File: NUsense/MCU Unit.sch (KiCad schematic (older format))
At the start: 40 parts

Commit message: Update NUsense Files
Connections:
- net GND: now also Y?.2 (GND1), Y?.4 (GND2)
- net USART1_TX: now reaches U?.101 (PA9)
- net USART1_RX: now reaches U?.102 (PA10)
- net JTMS_SWDIO: now reaches U?.105 (PA13)
- net JTCK_SWCLK: now reaches U?.109 (PA14)
- net JTDI: now reaches U?.110 (PA15)
- net USART3_TX: now reaches U?.111 (PC10)
- net USART3_RX: now reaches U?.112 (PC11)
- net UART5_TX: now reaches U?.113 (PC12)
- net JTDO_SWO: now reaches U?.133 (PB3)
- net OTG_HS_ULPI_D: now reaches U?.135 (PB5)
- net OTG_HS_ULPI_D: now also U?.37 (PA3), U?.46 (PB0), U?.47 (PB1), U?.69 (PB10), U?.70 (PB11), U?.73 (PB12), U?.74 (PB13)
- net MPU_SCL: now reaches U?.136 (PB6)
- net MPU_SDA/SDI: now reaches U?.137 (PB7)
- net MPU_INT: now reaches U?.139 (PB8)
- net OTG_HS_UPLI_STP: now reaches U?.26 (PC0)
- net OTG_HS_ULPI_DIR: now reaches U?.28 (PC2)
- net OTG_HS_UPLI_NXT: now reaches U?.29 (PC3)
- net OTG_HS_ULPI_CK: now reaches U?.41 (PA5)
- net USART6_TX: now reaches U?.96 (PC6)
- net USART6_RX: now reaches U?.97 (PC7)
- net UART5_RX: now reaches U?.116 (PD2)
- net USART2_TX: now reaches U?.119 (PD5)
- net USART2_RX: now reaches U?.122 (PD6)
- net UART8_RX: now reaches U?.141 (PE0)
- net UART8_TX: now reaches U?.142 (PE1)
- net UART7_RX: now reaches U?.58 (PE7)
- net UART7_TX: now reaches U?.59 (PE8)
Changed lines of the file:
@@
 LIBS:NUbots
 LIBS:STM32F746ZGT6
+LIBS:Header_Connectors
 LIBS:NUsense-cache
 EELAYER 25 0
@@
 $Descr A3 16535 11693
 encoding utf-8
-Sheet 3 4
+Sheet 3 9
 Title ""
 Date ""
@@
 	3800 6100 3800 5800
 Wire Wire Line
-	2850 6900 2700 6900
-Wire Wire Line
 	2700 6900 2700 7000
-Wire Wire Line
-	2600 7000 2850 7000
 Connection ~ 2700 7000
 Wire Wire Line
@@
 	1700 10100 3550 10100
 Connection ~ 3550 10100
+Text GLabel 5150 3200 0    60   Input ~ 0
+USART1_TX
+Text GLabel 5150 3300 0    60   Input ~ 0
+USART1_RX
+Text GLabel 6650 2900 2    60   Input ~ 0
+USART6_TX
+Text GLabel 6650 3000 2    60   Input ~ 0
+USART6_RX
+Text GLabel 6650 3300 2    60   Input ~ 0
+USART3_TX
+Text GLabel 6650 3400 2    60   Input ~ 0
+USART3_RX
+Text GLabel 6650 3500 2    60   Input ~ 0
+UART5_TX
+Text GLabel 12300 2500 0    60   Input ~ 0
+UART5_RX
+Text GLabel 12300 2800 0    60   Input ~ 0
+USART2_TX
+Text GLabel 12300 2900 0    60   Input ~ 0
+USART2_RX
+Text GLabel 12300 4000 0    60   Input ~ 0
+UART8_RX
+Text GLabel 12300 4100 0    60   Input ~ 0
+UART8_TX
+Text GLabel 12300 4700 0    60   Input ~ 0
+UART7_RX
+Text GLabel 12300 4800 0    60   Input ~ 0
+UART7_TX
+Text GLabel 5150 4600 0    60   Input ~ 0
+MPU_SCL
+Text GLabel 5150 4700 0    60   Input ~ 0
+MPU_SDA/SDI
+Text GLabel 5150 4800 0    60   Input ~ 0
+MPU_INT
+Text GLabel 5150 3600 0    60   Input ~ 0
+JTMS_SWDIO
+Text GLabel 5150 3700 0    60   Input ~ 0
+JTCK_SWCLK
+Text GLabel 5150 3800 0    60   Input ~ 0
+JTDI
+Text GLabel 5150 4300 0    60   Input ~ 0
+JTDO_SWO
+Text GLabel 5150 2600 0    60   Input ~ 0
+OTG_HS_ULPI_D
+Text GLabel 5150 4000 0    60   Input ~ 0
+OTG_HS_ULPI_D
+Text GLabel 5150 4100 0    60   Input ~ 0
+OTG_HS_ULPI_D
+Text GLabel 5150 4500 0    60   Input ~ 0
+OTG_HS_ULPI_D
+Text GLabel 5150 5000 0    60   Input ~ 0
+OTG_HS_ULPI_D
+Text GLabel 5150 5100 0    60   Input ~ 0
+OTG_HS_ULPI_D
+Text GLabel 5150 5200 0    60   Input ~ 0
+OTG_HS_ULPI_D
+Text GLabel 5150 5300 0    60   Input ~ 0
+OTG_HS_ULPI_D
+Text GLabel 5150 2800 0    60   Input ~ 0
+OTG_HS_ULPI_CK
+Text GLabel 6650 2300 2    60   Input ~ 0
+OTG_HS_UPLI_STP
+Text GLabel 6650 2500 2    60   Input ~ 0
+OTG_HS_ULPI_DIR
+Text GLabel 6650 2600 2    60   Input ~ 0
+OTG_HS_UPLI_NXT
+Wire Wire Line
+	2600 7000 2800 7000
+Wire Wire Line
+	2800 6900 2700 6900
 $EndSCHEMATC

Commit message: Change hierarchy layout
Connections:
- net JTDO_SWO renamed JTD0_SW0
- net MCU_NRESET renamed MCU_RESET
- net OTG_HS_UPLI_NXT renamed OTG_HS_ULPI_NXT
- net OTG_HS_UPLI_STP renamed OTG_HS_ULPI_STP
- net VDD3o3V renamed +3V3
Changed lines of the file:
@@
 LIBS:valves
 LIBS:ADM6713RAKS
+LIBS:Header_Connectors
 LIBS:MPU6000
 LIBS:NUbots
 LIBS:STM32F746ZGT6
-LIBS:Header_Connectors
 LIBS:NUsense-cache
 EELAYER 25 0
@@
 	0    -1   -1   0
 $EndComp
-Text GLabel 3250 7700 0    60   Input ~ 0
-MCU_NRESET
 $Comp
 L R R?
@@
 	1    0    0    -1
 $EndComp
-Text GLabel 5800 7500 2    60   Input ~ 0
-VDD3o3V
 $Comp
 L GND #PWR?
@@
 	1    0    0    -1
 $EndComp
-Text GLabel 6700 7000 1    60   Input ~ 0
-VDD3o3V
-Text GLabel 9200 8200 1    60   Input ~ 0
-VDD3o3V_MCU
 $Comp
 L Ferrite_Bead L?
@@
 	1    0    0    -1
 $EndComp
-Text GLabel 8250 8400 0    60   Input ~ 0
-VDD3o3V
 Text GLabel 8250 8850 0    60   Input ~ 0
 RTC_BAT
@@
 	0    1    1    0
 $EndComp
-Text GLabel 6900 9900 0    60   Input ~ 0
-VDD3o3V
 $Comp
 L GND #PWR?
@@
 	-1   0    0    1
 $EndComp
-Text GLabel 1300 9150 1    60   Input ~ 0
-VDD3o3V_MCU
 $Comp
 L GND #PWR?
@@
 	1700 10100 3550 10100
 Connection ~ 3550 10100
-Text GLabel 5150 3200 0    60   Input ~ 0
-USART1_TX
-Text GLabel 5150 3300 0    60   Input ~ 0
-USART1_RX
-Text GLabel 6650 2900 2    60   Input ~ 0
-USART6_TX
-Text GLabel 6650 3000 2    60   Input ~ 0
-USART6_RX
-Text GLabel 6650 3300 2    60   Input ~ 0
-USART3_TX
-Text GLabel 6650 3400 2    60   Input ~ 0
-USART3_RX
-Text GLabel 6650 3500 2    60   Input ~ 0
-UART5_TX
-Text GLabel 12300 2500 0    60   Input ~ 0
-UART5_RX
-Text GLabel 12300 2800 0    60   Input ~ 0
-USART2_TX
-Text GLabel 12300 2900 0    60   Input ~ 0
-USART2_RX
-Text GLabel 12300 4000 0    60   Input ~ 0
-UART8_RX
-Text GLabel 12300 4100 0    60   Input ~ 0
-UART8_TX
-Text GLabel 12300 4700 0    60   Input ~ 0
-UART7_RX
-Text GLabel 12300 4800 0    60   Input ~ 0
-UART7_TX
-Text GLabel 5150 4600 0    60   Input ~ 0
-MPU_SCL
-Text GLabel 5150 4700 0    60   Input ~ 0
-MPU_SDA/SDI
-Text GLabel 5150 4800 0    60   Input ~ 0
-MPU_INT
-Text GLabel 5150 3600 0    60   Input ~ 0
-JTMS_SWDIO
-Text GLabel 5150 3700 0    60   Input ~ 0
-JTCK_SWCLK
-Text GLabel 5150 3800 0    60   Input ~ 0
-JTDI
-Text GLabel 5150 4300 0    60   Input ~ 0
-JTDO_SWO
 Text GLabel 5150 2600 0    60   Input ~ 0
 OTG_HS_ULPI_D
@@
 Text GLabel 5150 5300 0    60   Input ~ 0
 OTG_HS_ULPI_D
-Text GLabel 5150 2800 0    60   Input ~ 0
+Wire Wire Line
+	2600 7000 2800 7000
+Wire Wire Line
+	2800 6900 2700 6900
+$Comp
+L +3.3V #PWR?
+U 1 1 5A6FCDF0
+P 6700 7000
+F 0 "#PWR?" H 6700 6850 50  0001 C CNN
+F 1 "+3.3V" H 6700 7140 50  0000 C CNN
+F 2 "" H 6700 7000 50  0001 C CNN
+F 3 "" H 6700 7000 50  0001 C CNN
+	1    6700 7000
+	1    0    0    -1
+$EndComp
+$Comp
+L +3.3V #PWR?
+U 1 1 5A6FCE7A
+P 5800 7500
+F 0 "#PWR?" H 5800 7350 50  0001 C CNN
+F 1 "+3.3V" H 5800 7640 50  0000 C CNN
+F 2 "" H 5800 7500 50  0001 C CNN
+F 3 "" H 5800 7500 50  0001 C CNN
+	1    5800 7500
+	0    1    1    0
+$EndComp
+$Comp
+L +3.3V #PWR?
+U 1 1 5A6FD08D
+P 6900 9900
+F 0 "#PWR?" H 6900 9750 50  0001 C CNN
+F 1 "+3.3V" H 6900 10040 50  0000 C CNN
+F 2 "" H 6900 9900 50  0001 C CNN
+F 3 "" H 6900 9900 50  0001 C CNN
+	1    6900 9900
+	0    -1   -1   0
+$EndComp
+$Comp
+L +3.3V #PWR?
+U 1 1 5A6FD2DC
+P 8250 8400
+F 0 "#PWR?" H 8250 8250 50  0001 C CNN
+F 1 "+3.3V" H 8250 8540 50  0000 C CNN
+F 2 "" H 8250 8400 50  0001 C CNN
+F 3 "" H 8250 8400 50  0001 C CNN
+	1    8250 8400
+	0    -1   -1   0
+$EndComp
+Text HLabel 5150 4800 0    60   Input ~ 0
+MPU_INT
+Text HLabel 5150 4700 0    60   Input ~ 0
+MPU_SDA/SDI
+Text HLabel 5150 4600 0    60   Input ~ 0
+MPU_SCL
+Text HLabel 3250 7700 0    60   Input ~ 0
+MCU_RESET
+Text HLabel 6650 2300 2    60   BiDi ~ 0
+OTG_HS_ULPI_STP
+Text HLabel 6650 2500 2    60   BiDi ~ 0
+OTG_HS_ULPI_DIR
+Text HLabel 6650 2600 2    60   BiDi ~ 0
+OTG_HS_ULPI_NXT
+Text HLabel 5150 2800 0    60   BiDi ~ 0
 OTG_HS_ULPI_CK
-Text GLabel 6650 2300 2    60   Input ~ 0
-OTG_HS_UPLI_STP
-Text GLabel 6650 2500 2    60   Input ~ 0
-OTG_HS_ULPI_DIR
-Text GLabel 6650 2600 2    60   Input ~ 0
-OTG_HS_UPLI_NXT
-Wire Wire Line
-	2600 7000 2800 7000
-Wire Wire Line
-	2800 6900 2700 6900
+Text Label 9200 8200 0    60   ~ 0
+VDD3o3V_MCU
+Text Label 1300 9150 0    60   ~ 0
+VDD3o3V_MCU
+Text HLabel 5150 4300 0    60   BiDi ~ 0
+JTD0_SW0
+Text HLabel 5150 3800 0    60   BiDi ~ 0
+JTDI
+Text HLabel 5150 3700 0    60   BiDi ~ 0
+JTCK_SWCLK
+Text HLabel 5150 3600 0    60   BiDi ~ 0
+JTMS_SWDIO
+Text HLabel 5150 3200 0    60   Output ~ 0
+USART1_TX
+Text HLabel 5150 3300 0    60   Input ~ 0
+USART1_RX
+Text HLabel 6650 2900 2    60   Output ~ 0
+USART6_TX
+Text HLabel 6650 3000 2    60   Input ~ 0
+USART6_RX
+Text HLabel 6650 3400 2    60   Input ~ 0
+USART3_RX
+Text HLabel 6650 3300 2    60   Output ~ 0
+USART3_TX
+Text HLabel 6650 3500 2    60   Output ~ 0
+UART5_TX
+Text HLabel 12300 2800 0    60   Output ~ 0
+USART2_TX
+Text HLabel 12300 2500 0    60   Input ~ 0
+UART5_RX
+Text HLabel 12300 4100 0    60   Output ~ 0
+UART8_TX
+Text HLabel 12300 2900 0    60   Input ~ 0
+USART2_RX
+Text HLabel 12300 4000 0    60   Input ~ 0
+UART8_RX
+Text HLabel 12300 4800 0    60   Output ~ 0
+UART7_TX
+Text HLabel 12300 4700 0    60   Input ~ 0
+UART7_RX
 $EndSCHEMATC

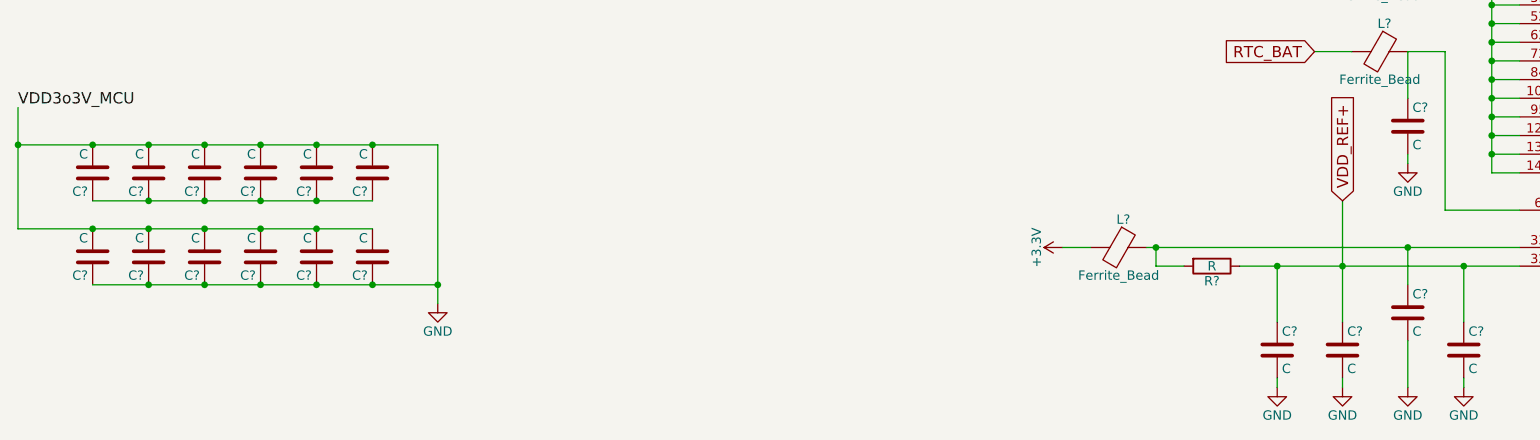
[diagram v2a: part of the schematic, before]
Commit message: Update Component Values
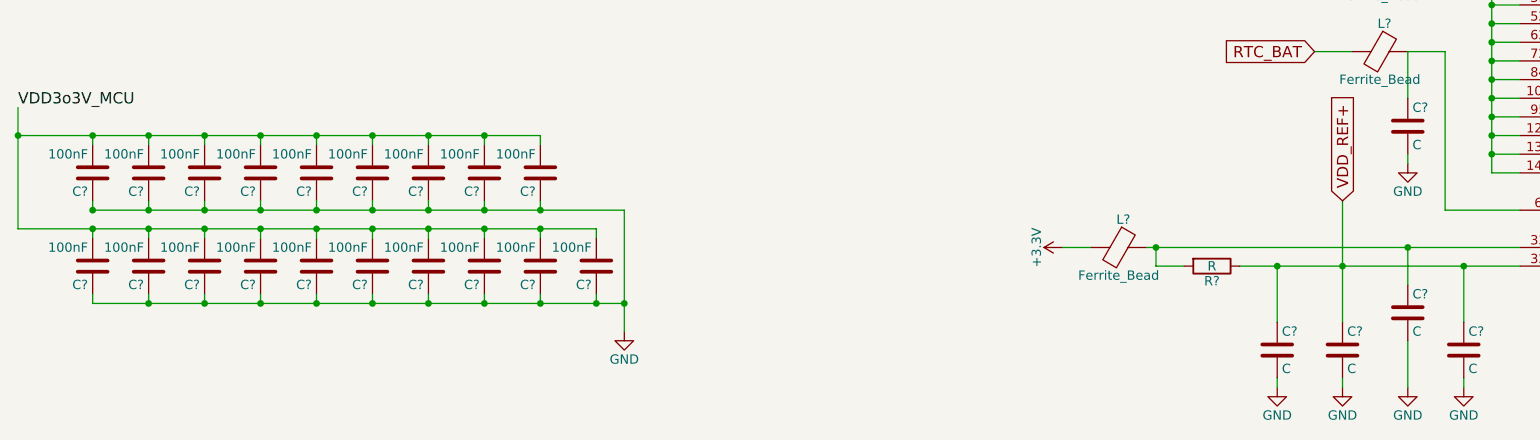
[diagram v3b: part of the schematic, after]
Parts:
- removed C? (x11): C, symbol C
- added C? (x18): 100nF, symbol C
- C?: value C -> 100nF
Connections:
- net GND: now also C?.1, C?.1, C?.1, C?.1, C?.1, C?.1, C?.1, C?.1, C?.1, C?.1, C?.1, C?.1, C?.1, C?.1, C?.1, C?.1, C?.1, C?.1; no longer C?.2, L?.1, U?.108 (VDD8), U?.121 (VDD10), U?.131 (VDD11), U?.144 (VDD12), U?.17 (VDD1), U?.30 (VDD2), U?.39 (VDD3), U?.52 (VDD4), U?.62 (VDD5), U?.72 (VDD6), U?.84 (VDD7), U?.95 (VDD9)
- new net VDD3o3V_MCU: C?.2, C?.2, C?.2, C?.2, C?.2, C?.2, C?.2, C?.2, C?.2, C?.2, C?.2, C?.2, C?.2, C?.2, C?.2, C?.2, C?.2, C?.2, C?.2, L?.1, U?.108 (VDD8), U?.121 (VDD10), U?.131 (VDD11), U?.144 (VDD12), U?.17 (VDD1), U?.30 (VDD2), U?.39 (VDD3), U?.52 (VDD4), U?.62 (VDD5), U?.72 (VDD6), U?.84 (VDD7), U?.95 (VDD9)
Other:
- moved on the sheet: C?
